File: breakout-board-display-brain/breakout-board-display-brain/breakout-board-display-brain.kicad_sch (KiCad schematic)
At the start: 9 parts, among them J1 Conn_01x19_Socket, J2 Conn_01x19_Socket, J3 Conn_01x16_Female, J4 Conn_01x17_Socket, J5 Conn_01x11_Socket, SW1 RotaryEncoder_Switch, U1 ESP32-WROOM-32

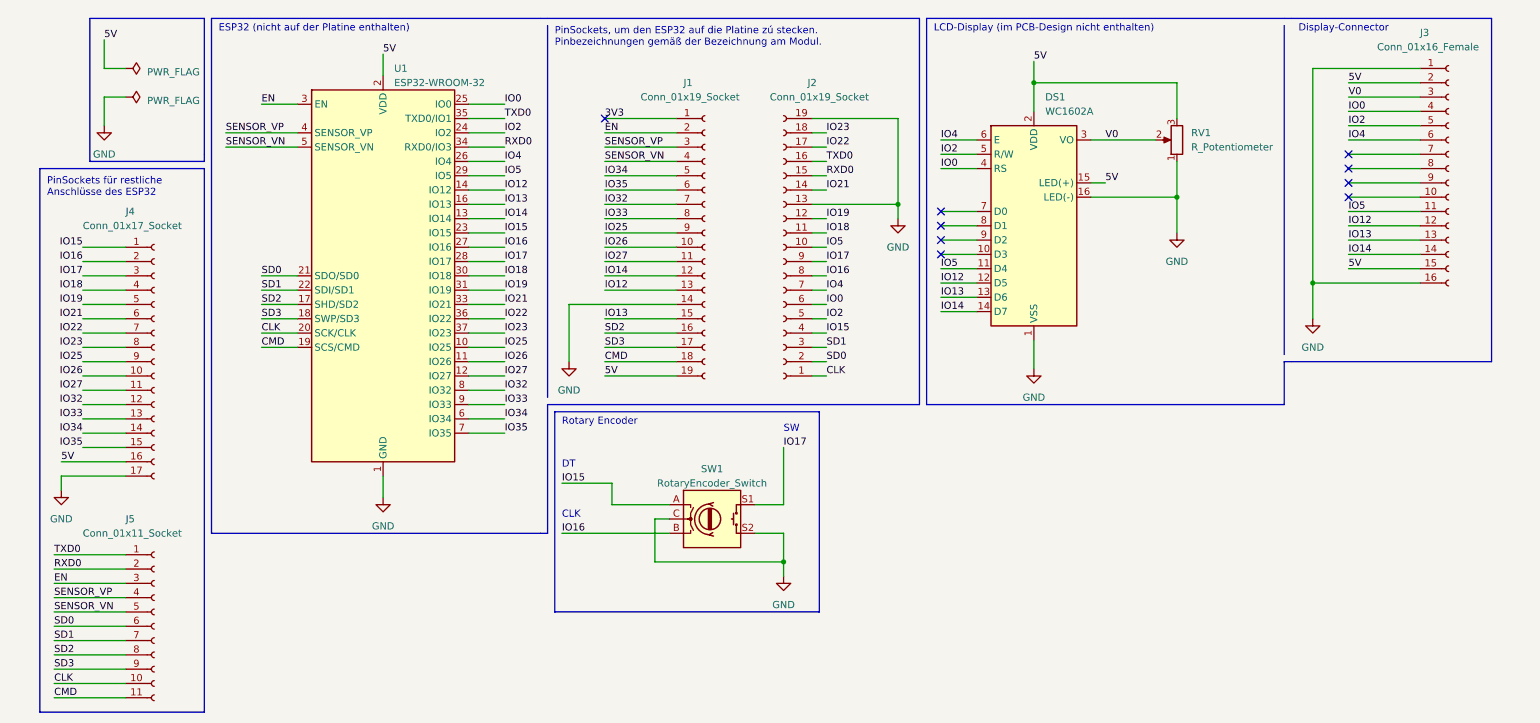
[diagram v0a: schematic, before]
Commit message: display-brain modified
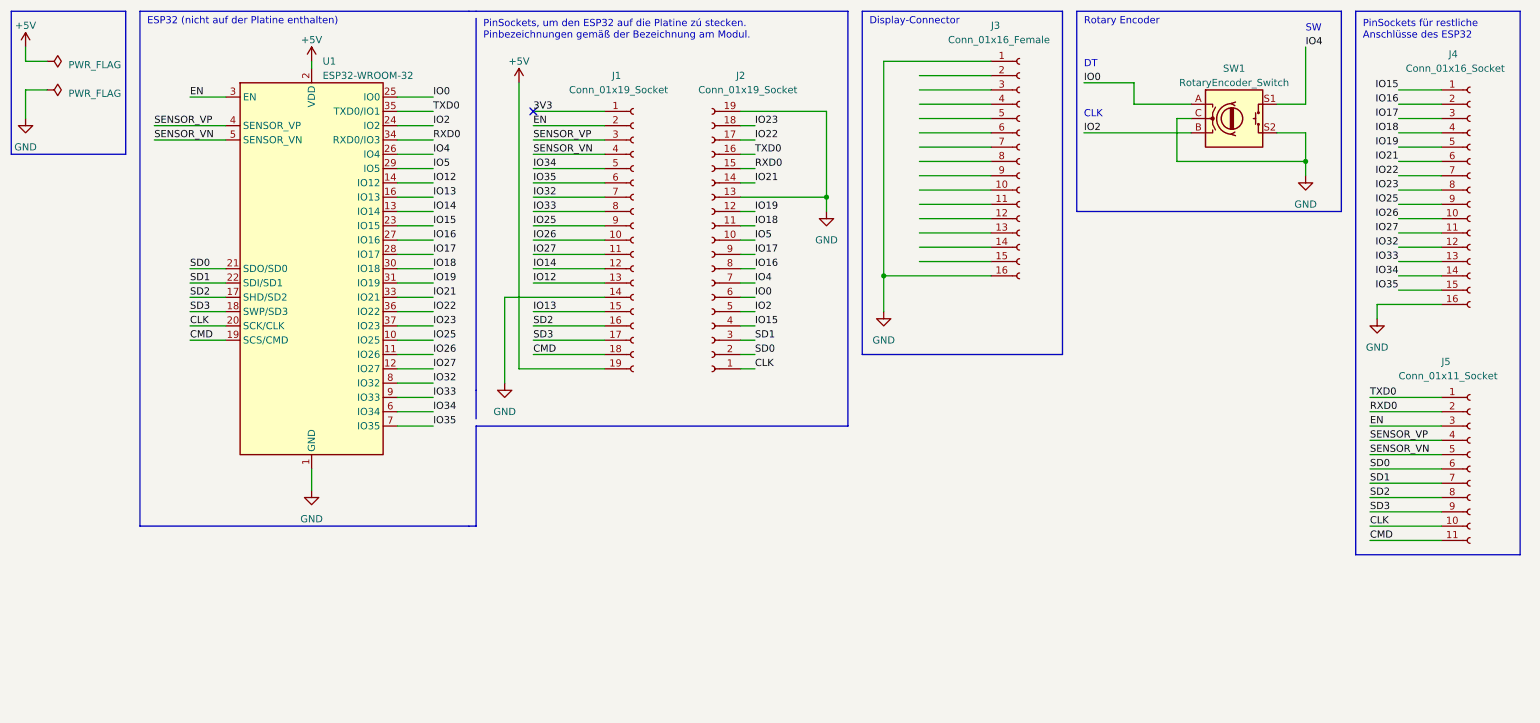
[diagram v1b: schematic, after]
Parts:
- removed DS1: WC1602A, Display:WC1602A, symbol Display_Character:WC1602A
- removed J4: Conn_01x17_Socket, symbol Connector:Conn_01x17_Socket
- removed RV1: R_Potentiometer, Potentiometer_THT:Potentiometer_ACP_CA9-V10_Vertical, symbol Device:R_Potentiometer
- added J4: Conn_01x16_Socket, symbol Connector:Conn_01x16_Socket
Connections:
- net GND: now also J4.16 (Pin_16)
- net IO0: now also SW1.A; no longer J3.4 (Pin_4)
- net IO12: no longer J3.12 (Pin_12)
- net IO13: no longer J3.13 (Pin_13)
- net IO14: no longer J3.14 (Pin_14)
- net IO15: now also J4.1 (Pin_1); no longer SW1.A
- net IO16: now also J4.2 (Pin_2); no longer SW1.B
- net IO17: now also J4.3 (Pin_3); no longer SW1.S1
- net IO18: now also J4.4 (Pin_4)
- net IO19: now also J4.5 (Pin_5)
- net IO2: now also SW1.B; no longer J3.5 (Pin_5)
- net IO21: now also J4.6 (Pin_6)
- net IO22: now also J4.7 (Pin_7)
- net IO23: now also J4.8 (Pin_8)
- net IO25: now also J4.9 (Pin_9)
- net IO26: now also J4.10 (Pin_10)
- net IO27: now also J4.11 (Pin_11)
- net IO32: now also J4.12 (Pin_12)
- net IO33: now also J4.13 (Pin_13)
- net IO34: now also J4.14 (Pin_14)
- net IO35: now also J4.15 (Pin_15)
- net IO4: now also SW1.S1; no longer J3.6 (Pin_6)
- net IO5: no longer J3.11 (Pin_11)
- net 5V renamed +5V
- net +5V: no longer J3.15 (Pin_15), J3.2 (Pin_2)
- net V0: no longer names the net of J3.3 (Pin_3)
- no-connect marks 9 -> 1
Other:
- note removed: "LCD-Display (im PCB-Design nicht enthalten)"
- moved on the sheet: J1, J2, J3, J5, SW1, U1

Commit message: finsihed breakout-board.display-brain
fertig fürs Fräsen
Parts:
- removed J3: Conn_01x16_Female, Connector_PinSocket_2.54mm:PinSocket_1x16_P2.54mm_Vertical, symbol Connector:Conn_01x16_Female
- removed J4: Conn_01x16_Socket, symbol Connector:Conn_01x16_Socket
- removed J5: Conn_01x11_Socket, symbol Connector:Conn_01x11_Socket
- added J3: Conn_01x02_Socket, Connector_PinSocket_2.54mm:PinSocket_1x02_P2.54mm_Vertical, symbol Connector:Conn_01x02_Socket
- added J4: Conn_01x04_Socket, Connector_PinSocket_2.54mm:PinSocket_1x04_P2.54mm_Vertical, symbol Connector:Conn_01x04_Socket
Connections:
- net +5V: now also J3.1 (Pin_1), J4.2 (Pin_2)
- net GND: now also J3.2 (Pin_2), J4.1 (Pin_1)
- net IO0: now also SW1.B; no longer SW1.A
- net IO2: now also SW1.A; no longer SW1.B
- net IO18 renamed IO18_SCK
- net IO19 renamed IO19_MISO
- net IO21 renamed IO21_SDA
- net IO21_SDA: now also J4.3 (Pin_3)
- net IO22 renamed IO22_SCL
- net IO22_SCL: now also J4.4 (Pin_4)
- net IO23 renamed IO23_MOSI
- net IO5 renamed IO5_SS
- no-connect marks 1 -> 29
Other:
- note added: "Display Connector"
- note added: "Power Connector"
- note removed: "Display-Connector"
- note removed: "PinSockets für restliche Anschlüsse des ESP32"
- moved on the sheet: J1, J2, SW1

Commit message: plot files generated for manufacturing
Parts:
- added J5: Conn_01x04_Socket, Connector_PinSocket_2.54mm:PinSocket_1x04_P2.54mm_Vertical, symbol Connector:Conn_01x04_Socket
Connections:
- net IO18_SCK: now also J5.3 (Pin_3)
- net IO19_MISO: now also J5.2 (Pin_2)
- net IO23_MOSI: now also J5.1 (Pin_1)
- net IO5_SS: now also J5.4 (Pin_4)
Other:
- note added: "Receiver Connector"
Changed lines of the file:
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@@
+    (stroke (width 0) (type default))
+  )
+  (polyline (pts (xy 222.25 55.88) (xy 222.25 40.64))
     (stroke (width 0) (type default))
   )
@@
     (stroke (width 0) (type default))
   )
+  (polyline (pts (xy 261.62 40.64) (xy 261.62 55.88))
+    (stroke (width 0) (type default))
+  )
   (polyline (pts (xy 95.25 105.41) (xy 36.83 105.41))
     (stroke (width 0) (type default))
@@
     (stroke (width 0) (type default))
   )
+  (wire (pts (xy 223.52 48.26) (xy 234.95 48.26))
+    (stroke (width 0) (type default))
+  )
   (polyline (pts (xy 13.97 13.97) (xy 13.97 39.37))
     (stroke (width 0) (type default))
@@
     (stroke (width 0) (type default))
   )
+  (wire (pts (xy 223.52 45.72) (xy 234.95 45.72))
+    (stroke (width 0) (type default))
+  )
   (wire (pts (xy 82.55 49.53) (xy 88.9 49.53))
     (stroke (width 0) (type default))
@@
     (stroke (width 0) (type default))
   )
+  (polyline (pts (xy 222.25 40.64) (xy 261.62 40.64))
+    (stroke (width 0) (type default))
+  )
   (wire (pts (xy 20.32 27.94) (xy 16.51 27.94))
     (stroke (width 0) (type default))
@@
     (stroke (width 0) (type default))
   )
+  (wire (pts (xy 223.52 50.8) (xy 234.95 50.8))
+    (stroke (width 0) (type default))
+  )
   (wire (pts (xy 110.49 52.07) (xy 123.19 52.07))
     (stroke (width 0) (type default))
@@
     (stroke (width 0) (type default))
   )
+  (polyline (pts (xy 261.62 55.88) (xy 222.25 55.88))
+    (stroke (width 0) (type default))
+  )
   (wire (pts (xy 110.49 59.69) (xy 123.19 59.69))
     (stroke (width 0) (type default))
@@
     (stroke (width 0) (type default))
   )
+  (wire (pts (xy 223.52 53.34) (xy 234.95 53.34))
+    (stroke (width 0) (type default))
+  )
   (wire (pts (xy 147.32 54.61) (xy 149.86 54.61))
     (stroke (width 0) (type default))
@@
   )
   (text "Display Connector\n" (at 168.91 54.61 0)
+    (effects (font (size 1.27 1.27)) (justify left bottom))
+  )
+  (text "Receiver Connector" (at 223.52 43.18 0)
     (effects (font (size 1.27 1.27)) (justify left bottom))
   )
@@
     (effects (font (size 1.27 1.27)) (justify left bottom))
   )
+  (label "IO19_MISO" (at 223.52 48.26 0) (fields_autoplaced)
+    (effects (font (size 1.27 1.27)) (justify left bottom))
+  )
   (label "CMD" (at 110.49 74.93 0) (fields_autoplaced)
     (effects (font (size 1.27 1.27)) (justify left bottom))
@@
     (effects (font (size 1.27 1.27)) (justify left bottom))
   )
+  (label "IO18_SCK" (at 223.52 50.8 0) (fields_autoplaced)
+    (effects (font (size 1.27 1.27)) (justify left bottom))
+  )
   (label "IO0" (at 88.9 29.21 0) (fields_autoplaced)
     (effects (font (size 1.27 1.27)) (justify left bottom))
@@
     (effects (font (size 1.27 1.27)) (justify left bottom))
   )
+  (label "IO23_MOSI" (at 223.52 45.72 0) (fields_autoplaced)
+    (effects (font (size 1.27 1.27)) (justify left bottom))
+  )
   (label "SD3" (at 110.49 72.39 0) (fields_autoplaced)
     (effects (font (size 1.27 1.27)) (justify left bottom))
@@
   )
   (label "EN" (at 110.49 34.29 0) (fields_autoplaced)
+    (effects (font (size 1.27 1.27)) (justify left bottom))
+  )
+  (label "IO5_SS" (at 223.52 53.34 0) (fields_autoplaced)
     (effects (font (size 1.27 1.27)) (justify left bottom))
   )
@@
         )
       )
+    )
+  )
+  (symbol (lib_id "Connector:Conn_01x04_Socket") (at 240.03 48.26 0) (unit 1)
+    (in_bom yes) (on_board yes) (dnp no) (fields_autoplaced)
+    (property "Reference" "J5" (at 241.3 48.895 0)
+      (effects (font (size 1.27 1.27)) (justify left))
+    )
+    (property "Value" "Conn_01x04_Socket" (at 241.3 51.435 0)
+      (effects (font (size 1.27 1.27)) (justify left))
+    )
+    (property "Footprint" "Connector_PinSocket_2.54mm:PinSocket_1x04_P2.54mm_Vertical" (at 240.03 48.26 0)
+      (effects (font (size 1.27 1.27)) hide)
+    )
+    (property "Datasheet" "~" (at 240.03 48.26 0)
+      (effects (font (size 1.27 1.27)) hide)
+    )
+    (pin "1")
+    (pin "2")
+    (pin "3")
+    (pin "4")
+    (instances
+      (project "breakout-board-display-brain"
+        (path "/860671aa-4c8a-4921-a8d3-0a28e74ec70f"
+          (reference "J5") (unit 1)
+        )
+      )

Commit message: ...
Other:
- note added: "PinSockets, um den ESP32 auf die Platine zu stecken. Pinbezeichnungen gemäß der Bezeichnung am Modul."
- note removed: "PinSockets, um den ESP32 auf die Platine zú stecken. Pinbezeichnungen gemäß der Bezeichnung am Modul."
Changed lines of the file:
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@@
     (effects (font (size 1.27 1.27)) (justify left bottom))
   )
-  (text "PinSockets, um den ESP32 auf die Platine zú stecken.\nPinbezeichnungen gemäß der Bezeichnung am Modul."
+  (text "PinSockets, um den ESP32 auf die Platine zu stecken.\nPinbezeichnungen gemäß der Bezeichnung am Modul."
     (at 101.6 19.05 0)
     (effects (font (size 1.27 1.27)) (justify left bottom))
